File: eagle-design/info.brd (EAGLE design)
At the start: 57.2 x 64.4 mm, 17 parts

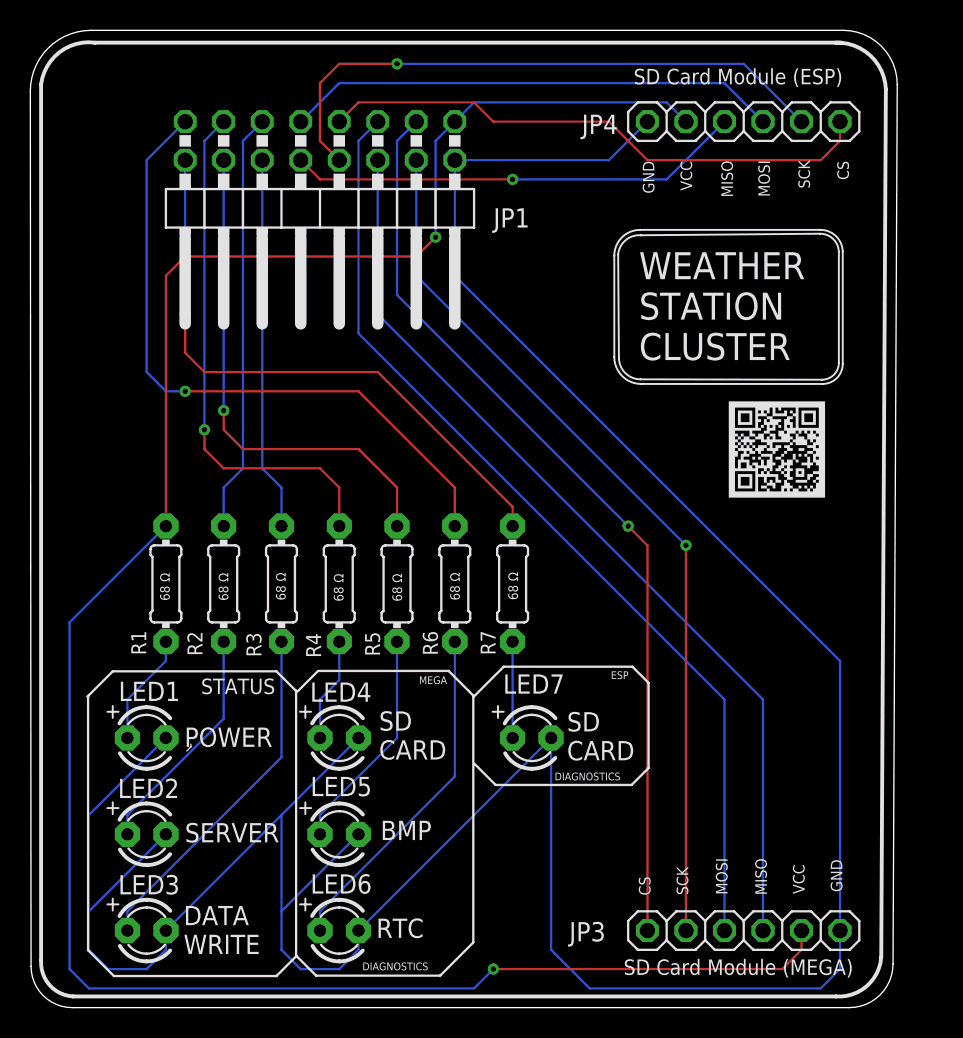
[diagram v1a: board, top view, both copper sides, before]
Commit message: Added motherboard design and image exports
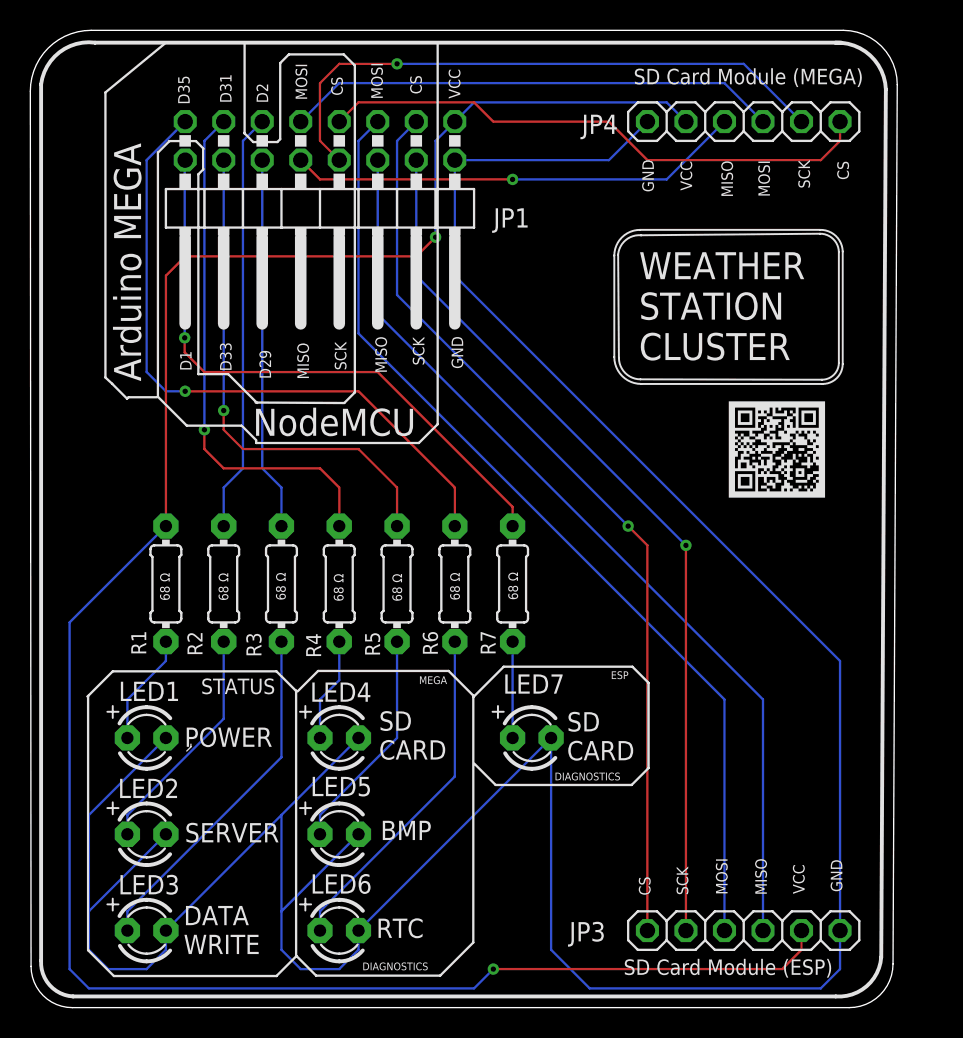
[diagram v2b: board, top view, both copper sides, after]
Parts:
- R1, R2, R3, R4, R5, R6, R7: value (none) -> 68
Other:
- board text added: "Arduino MEGA"
- board text added: "D1"
- board text added: "D2"
- board text added: "D29"
- board text added: "D31"
- board text added: "D33"
- board text added: "D35"
- board text added: "NodeMCU"
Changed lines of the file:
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@@
 <drawing>
 <settings>
-<setting alwaysvectorfont="no"/>
+<setting alwaysvectorfont="yes"/>
 <setting verticaltext="up"/>
 </settings>
@@
 <text x="91.1606" y="52.7812" size="0.508" layer="21">MEGA</text>
 <text x="103.8098" y="53.1114" size="0.508" layer="21">ESP</text>
-<text x="104.648" y="33.6042" size="1.016" layer="21">SD Card Module (MEGA)</text>
-<text x="105.3084" y="92.329" size="1.016" layer="21">SD Card Module (ESP)</text>
+<text x="104.648" y="33.6042" size="1.016" layer="21">SD Card Module (ESP)</text>
+<text x="105.3084" y="92.329" size="1.016" layer="21">SD Card Module (MEGA)</text>
 <text x="119.0752" y="39.0652" size="0.762" layer="21" rot="R90">GND</text>
 <text x="116.586" y="38.9382" size="0.762" layer="21" rot="R90">VCC</text>
@@
 <text x="108.9152" y="38.862" size="0.762" layer="21" rot="R90">SCK</text>
 <text x="106.426" y="38.8366" size="0.762" layer="21" rot="R90">CS</text>
-<text x="105.918" y="87.2744" size="0.762" layer="21" rot="R270">GND</text>
+<text x="105.88625" y="87.36965" size="0.762" layer="21" rot="R270">GND</text>
 <text x="108.4072" y="87.2744" size="0.762" layer="21" rot="R270">VCC</text>
 <text x="111.0996" y="87.2998" size="0.762" layer="21" rot="R270">MISO</text>
@@
 <rectangle x1="111.586009375" y1="71.358253125" x2="117.936009375" y2="71.390003125" layer="21"/>
 <rectangle x1="111.586009375" y1="71.390003125" x2="117.936009375" y2="71.421753125" layer="21"/>
+<text x="93.31325" y="75.7174" size="0.762" layer="21" rot="R270">GND</text>
+<text x="93.12275" y="93.33865" size="0.762" layer="21" rot="R270">VCC</text>
+<text x="91.34475" y="91.6686" size="0.762" layer="21" rot="R90">CS</text>
+<text x="91.5162" y="73.787" size="0.762" layer="21" rot="R90">SCK</text>
+<text x="88.773" y="91.3384" size="0.762" layer="21" rot="R90">MOSI</text>
+<text x="89.04605" y="73.279" size="0.762" layer="21" rot="R90">MISO</text>
+<text x="86.13775" y="91.57335" size="0.762" layer="21" rot="R90">CS</text>
+<text x="86.3727" y="73.4695" size="0.762" layer="21" rot="R90">SCK</text>
+<text x="83.02625" y="93.70695" size="0.762" layer="21" rot="R270">MOSI</text>
+<text x="83.90255" y="72.86625" size="0.762" layer="21" rot="R90">MISO</text>
+<text x="80.4545" y="92.4052" size="0.762" layer="21" rot="R270">D2</text>
+<text x="80.645" y="74.8157" size="0.762" layer="21" rot="R270">D29</text>
+<text x="78.0415" y="93.00845" size="0.762" layer="21" rot="R270">D31</text>
+<text x="78.0415" y="75.3237" size="0.762" layer="21" rot="R270">D33</text>
+<text x="75.27925" y="92.9132" size="0.762" layer="21" rot="R270">D35</text>
+<text x="75.40625" y="74.7522" size="0.762" layer="21" rot="R270">D1</text>
+<wire x1="79.629" y1="89.12225" x2="79.66075" y2="89.0905" width="0.1524" layer="21"/>
+<wire x1="79.66075" y1="89.0905" x2="80.23225" y2="88.519" width="0.1524" layer="21"/>
+<wire x1="80.23225" y1="88.519" x2="81.81975" y2="88.519" width="0.1524" layer="21"/>
+<wire x1="81.81975" y1="88.519" x2="82.01025" y2="88.7095" width="0.1524" layer="21"/>
+<wire x1="82.01025" y1="88.7095" x2="82.01025" y2="93.726" width="0.1524" layer="21"/>
+<wire x1="82.01025" y1="93.726" x2="82.58175" y2="94.2975" width="0.1524" layer="21"/>
+<wire x1="82.58175" y1="94.2975" x2="86.20125" y2="94.2975" width="0.1524" layer="21"/>
+<wire x1="86.20125" y1="94.2975" x2="86.9315" y2="93.56725" width="0.1524" layer="21"/>
+<wire x1="79.66075" y1="89.0905" x2="79.66075" y2="95.0595" width="0.1524" layer="21"/>
+<wire x1="86.9315" y1="93.56725" x2="86.9315" y2="72.009" width="0.1524" layer="21"/>
+<wire x1="86.9315" y1="72.009" x2="86.233" y2="71.3105" width="0.1524" layer="21"/>
+<wire x1="86.233" y1="71.3105" x2="80.391" y2="71.34225" width="0.1524" layer="21"/>
+<wire x1="80.42275" y1="68.67525" x2="91.15425" y2="68.67525" width="0.1524" layer="21"/>
+<wire x1="91.15425" y1="68.67525" x2="92.3925" y2="69.9135" width="0.1524" layer="21"/>
+<wire x1="92.3925" y1="69.9135" x2="92.3925" y2="95.0595" width="0.1524" layer="21"/>
+<text x="80.2005" y="69.1515" size="1.778" layer="21">NodeMCU</text>
+<wire x1="80.48625" y1="71.3105" x2="78.58125" y2="73.2155" width="0.1524" layer="21"/>
+<wire x1="78.58125" y1="73.2155" x2="76.61275" y2="73.2155" width="0.1524" layer="21"/>
+<wire x1="76.61275" y1="73.2155" x2="76.61275" y2="86.39175" width="0.1524" layer="21"/>
+<wire x1="76.61275" y1="86.39175" x2="76.93025" y2="86.70925" width="0.1524" layer="21"/>
+<wire x1="76.93025" y1="86.70925" x2="76.93025" y2="88.10625" width="0.1524" layer="21"/>
+<wire x1="76.93025" y1="88.10625" x2="76.454" y2="88.5825" width="0.1524" layer="21"/>
+<wire x1="76.454" y1="88.5825" x2="74.70775" y2="88.5825" width="0.1524" layer="21"/>
+<wire x1="74.70775" y1="88.5825" x2="73.94575" y2="87.8205" width="0.1524" layer="21"/>
+<wire x1="73.94575" y1="87.8205" x2="73.94575" y2="71.72325" width="0.1524" layer="21"/>
+<wire x1="73.94575" y1="71.72325" x2="75.85075" y2="69.81825" width="0.1524" layer="21"/>
+<wire x1="75.85075" y1="69.81825" x2="79.47025" y2="69.81825" width="0.1524" layer="21"/>
+<wire x1="79.47025" y1="69.81825" x2="80.42275" y2="68.86575" width="0.1524" layer="21"/>
+<wire x1="80.42275" y1="68.86575" x2="80.42275" y2="68.67525" width="0.1524" layer="21"/>
+<wire x1="73.88225" y1="71.6915" x2="72.009" y2="71.6915" width="0.1524" layer="21"/>
+<wire x1="72.009" y1="71.6915" x2="71.91375" y2="71.59625" width="0.1524" layer="21"/>
+<wire x1="71.91375" y1="71.59625" x2="70.9295" y2="72.5805" width="0.1524" layer="21"/>
+<wire x1="70.9295" y1="72.5805" x2="70.485" y2="72.99325" width="0.1524" layer="21"/>
+<wire x1="70.485" y1="72.99325" x2="70.485" y2="91.78925" width="0.1524" layer="21"/>
+<wire x1="70.485" y1="91.78925" x2="74.422" y2="95.02775" width="0.1524" layer="21"/>
+<text x="72.8345" y="72.73925" size="1.778" layer="21" rot="R90">Arduino MEGA</text>
 </plain>
 <attributes>
@@
 <attribute name="VALUE" x="100.5078" y="47.5742" size="1.27" layer="27" ratio="10"/>
 </element>
-<element name="R1" library="adafruit" package="0204/7" value="" x="74.4728" y="59.3852" smashed="yes" rot="R90">
+<element name="R1" library="adafruit" package="0204/7" value="68" x="74.4728" y="59.3852" smashed="yes" rot="R90">
 <attribute name="NAME" x="73.1774" y="54.6862" size="0.9906" layer="25" ratio="12" rot="R90"/>
 <attribute name="VALUE" x="74.9554" y="57.7596" size="0.9906" layer="27" ratio="12" rot="R90"/>
 </element>
-<element name="R2" library="adafruit" package="0204/7" value="" x="78.2828" y="59.3852" smashed="yes" rot="R90">
+<element name="R2" library="adafruit" package="0204/7" value="68" x="78.2828" y="59.3852" smashed="yes" rot="R90">
 <attribute name="NAME" x="76.8858" y="54.6354" size="0.9906" layer="25" ratio="12" rot="R90"/>
 <attribute name="VALUE" x="78.7654" y="57.7596" size="0.9906" layer="27" ratio="12" rot="R90"/>
 </element>
-<element name="R3" library="adafruit" package="0204/7" value="" x="82.0928" y="59.3852" smashed="yes" rot="R90">
+<element name="R3" library="adafruit" package="0204/7" value="68" x="82.0928" y="59.3852" smashed="yes" rot="R90">
 <attribute name="NAME" x="80.772" y="54.5592" size="0.9906" layer="25" ratio="12" rot="R90"/>
 <attribute name="VALUE" x="82.5754" y="57.7596" size="0.9906" layer="27" ratio="12" rot="R90"/>
 </element>
-<element name="R4" library="adafruit" package="0204/7" value="" x="85.9028" y="59.3852" smashed="yes" rot="R90">
+<element name="R4" library="adafruit" package="0204/7" value="68" x="85.9028" y="59.3852" smashed="yes" rot="R90">
 <attribute name="NAME" x="84.709" y="54.5084" size="0.9906" layer="25" ratio="12" rot="R90"/>
 <attribute name="VALUE" x="86.3854" y="57.7596" size="0.9906" layer="27" ratio="12" rot="R90"/>
 </element>
-<element name="R5" library="adafruit" package="0204/7" value="" x="89.7128" y="59.3852" smashed="yes" rot="R90">
+<element name="R5" library="adafruit" package="0204/7" value="68" x="89.7128" y="59.3852" smashed="yes" rot="R90">
 <attribute name="NAME" x="88.5952" y="54.61" size="0.9906" layer="25" ratio="12" rot="R90"/>
 <attribute name="VALUE" x="90.1954" y="57.7596" size="0.9906" layer="27" ratio="12" rot="R90"/>
 </element>
-<element name="R6" library="adafruit" package="0204/7" value="" x="93.5228" y="59.3852" smashed="yes" rot="R90">
+<element name="R6" library="adafruit" package="0204/7" value="68" x="93.5228" y="59.3852" smashed="yes" rot="R90">
 <attribute name="NAME" x="92.4052" y="54.6608" size="0.9906" layer="25" ratio="12" rot="R90"/>
 <attribute name="VALUE" x="94.0054" y="57.7596" size="0.9906" layer="27" ratio="12" rot="R90"/>
 </element>
-<element name="R7" library="adafruit" package="0204/7" value="" x="97.3328" y="59.3852" smashed="yes" rot="R90">
+<element name="R7" library="adafruit" package="0204/7" value="68" x="97.3328" y="59.3852" smashed="yes" rot="R90">
 <attribute name="NAME" x="96.2152" y="54.6862" size="0.9906" layer="25" ratio="12" rot="R90"/>
 <attribute name="VALUE" x="97.8154" y="57.7596" size="0.9906" layer="27" ratio="12" rot="R90"/>
@@
 <wire x1="97.3328" y1="64.4652" x2="88.4428" y2="73.3552" width="0.1524" layer="1"/>
 <wire x1="88.4428" y1="73.3552" x2="77.0128" y2="73.3552" width="0.1524" layer="1"/>
-<wire x1="77.0128" y1="73.3552" x2="75.7428" y2="74.6252" width="0.1524" layer="1"/>
-<wire x1="75.7428" y1="74.6252" x2="75.7428" y2="77.1652" width="0.1524" layer="1"/>
-<via x="75.7428" y="77.1652" extent="1-16" drill="0.35"/>
-<wire x1="75.7428" y1="87.3252" x2="75.7428" y2="77.1652" width="0.1524" layer="16"/>
+<wire x1="77.0128" y1="73.3552" x2="75.71105" y2="74.65695" width="0.1524" layer="1"/>
+<wire x1="75.71105" y1="74.65695" x2="75.71105" y2="75.60945" width="0.1524" layer="1"/>
+<via x="75.71105" y="75.60945" extent="1-16" drill="0.35"/>
+<wire x1="75.7428" y1="87.3252" x2="75.71105" y2="87.29345" width="0.1524" layer="16"/>
+<wire x1="75.71105" y1="87.29345" x2="75.71105" y2="75.60945" width="0.1524" layer="16"/>
 </signal>
 </signals>

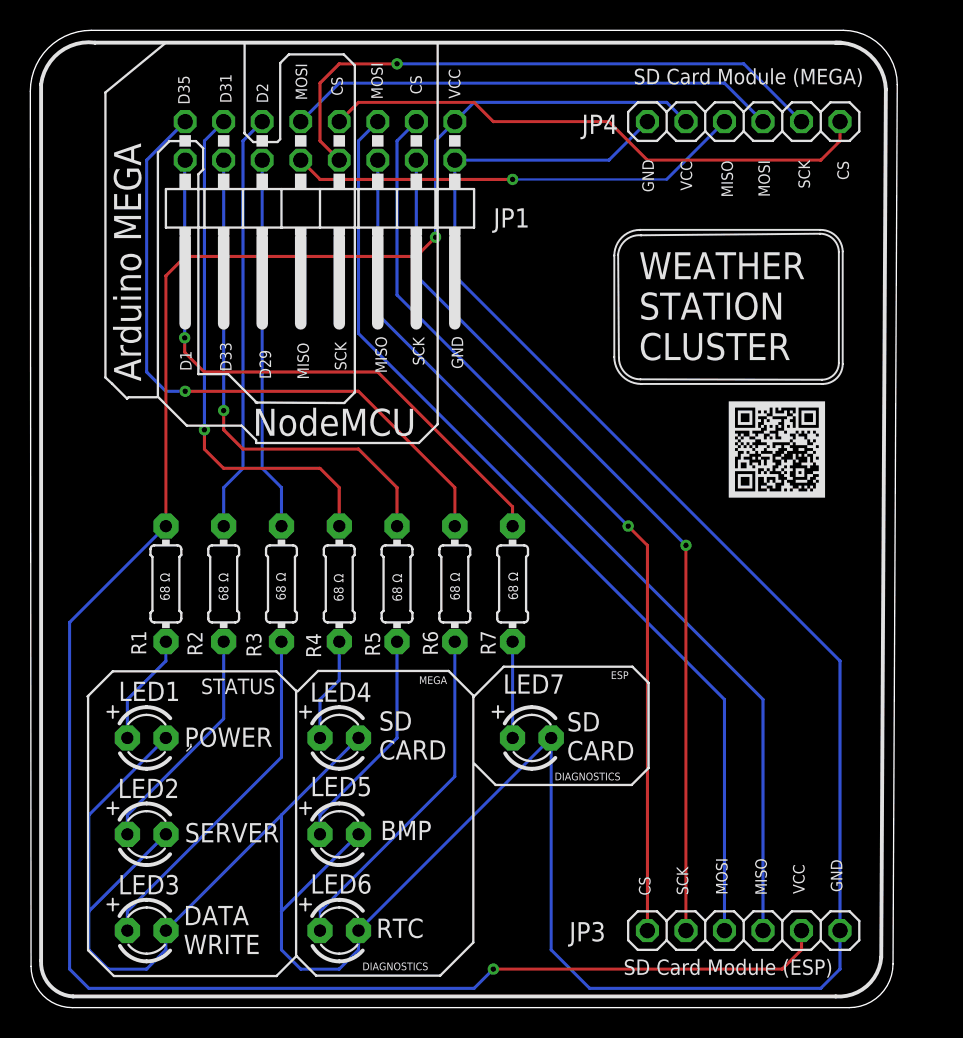
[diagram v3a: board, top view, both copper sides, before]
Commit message: Updated board design
Increased track width
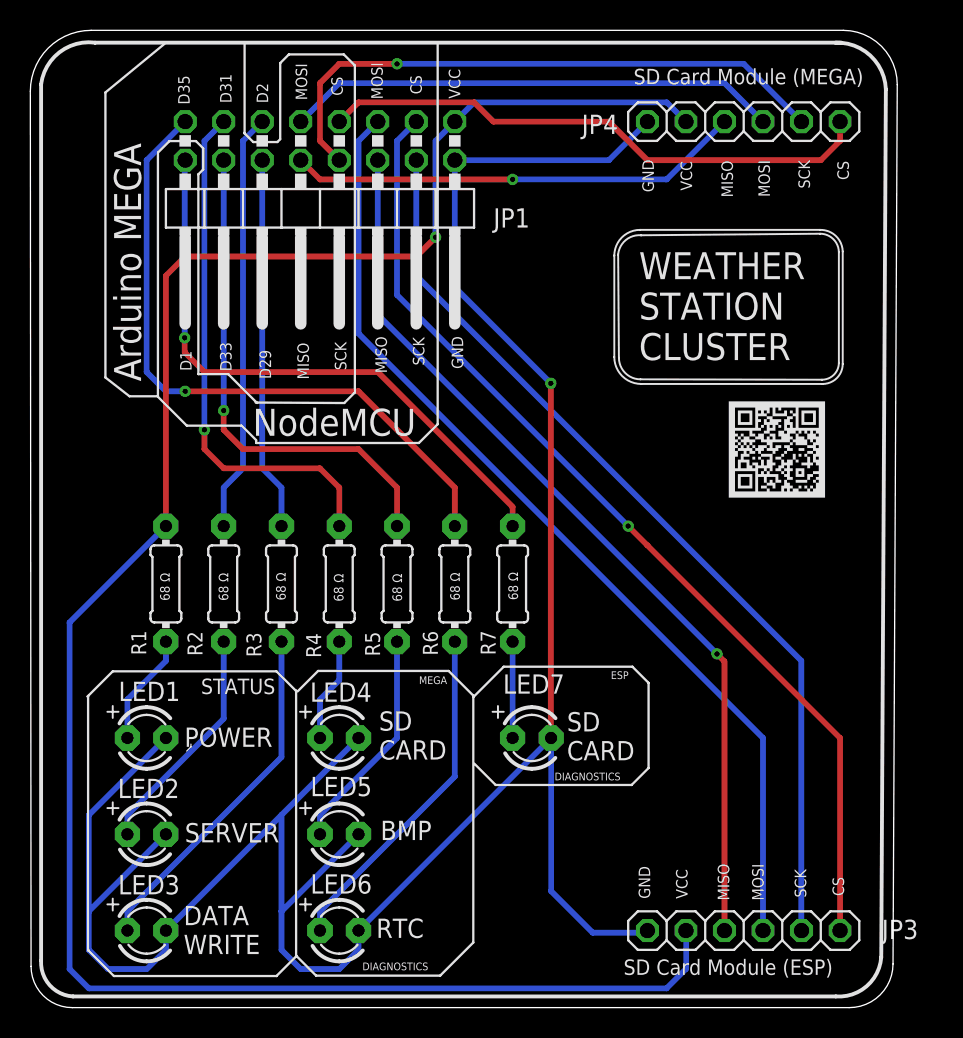
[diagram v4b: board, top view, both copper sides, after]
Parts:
- turned JP3 to 180 degrees
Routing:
- net N$9: track 202.3 -> 162.2 mm, vias 0 -> 1
- net N$11: track 142.7 -> 135.9 mm, vias 2 -> 1
- net N$12: track 60.7 -> 66.0 mm
- net N$13: track 58.2 -> 61.3 mm, vias 1 -> 0
- net N$15: track 61.3 -> 60.3 mm, vias 0 -> 1
- net N$14: track 63.9 -> 64.9 mm
